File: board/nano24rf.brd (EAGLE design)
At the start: 17.8 x 50 mm, 26 parts, among them CN1 1X4-CLEANBIG, CN2 1X4-CLEANBIG, CN3 1X4-CLEANBIG, CN4 1X4-CLEANBIG

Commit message: before route
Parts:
- removed C1, C2: (no value), ATTAMI-V0.00:0805
- removed CN1, CN2, CN3, CN4, I2CPORT: 1X4-CLEANBIG, adafruit:1X04-CLEANBIG
- removed FET1, FET2, JP6: (no value), ATTAMI-V0.00:1X02_ROUND
- removed SJ1: JUMPER-PAD-3-2OF3_NC_BY_TRACE_SMALL, ATTAMI-V0.00:PAD-JUMPER-3-2OF3_NC_BY_TRACE_YES_SILK_FULL_BOX
- removed SJ2: (no value), ATTAMI-V0.00:PAD-JUMPER-3-2OF3_NC_BY_TRACE_YES_SILK_FULL_BOX
- removed SW1: (no value), microbuilder:SPST_SMT_19192
- removed U$2: NRF24, ATTAMI-V0.00:NRF24-2X4
- removed U2: (no value), microbuilder:SOT23-WIDE
- added D3, D4: (no value), dp_devices:DO-214AC
- added Q3, Q4: (no value), adafruit:SOT23-W
- added R5, R6: (no value), ATTAMI-V0.00:0805
- added U$6, U$8: 1X3SMD, nanorf24:FATPAD
- added U$7: 1X7-SMDPADS, nanorf24:SMD1,27-2,54
- JP3: device adafruit:1X01-CLEANBIG -> pinhead+:2X03_SMT
- moved R4 27.0 mm to (11.7, 45.8), turned to 0 degrees
- moved R3 26.3 mm to (6.48, 49.8), turned to 0 degrees
- moved R1 25.9 mm to (5.08, 38.7), turned to 0 degrees
- moved R2 23.7 mm to (12.6, 36.4), turned to 0 degrees
- moved Q1 23.2 mm to (5.08, 35.6)
- moved Q2 20.9 mm to (12.6, 33.3)
- moved JP3 14.4 mm to (8.89, 18.9)
- moved JP1 10.2 mm to (1.27, 38.0)
- moved JP2 10.2 mm to (16.5, 38.0)
- moved D2 5.44 mm to (10.2, 5.08), turned to 90 degrees
- moved D1 4.02 mm to (14.0, 5.08), turned to 90 degrees
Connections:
- removed net IRQ: U$2.IRQ
- removed net N$1 (its old number): D1.2, FET1.2, Q1.3
- removed net RAW: JP3.1, JP6.1, SW1.B
- removed net RX: CN4.3, JP2.14
- removed net TX: CN4.2, JP2.15
- removed net V-ADJ: C2.1, SJ1.1, U2.2
- removed net V-NRF: SJ1.2, U$2.VCC
- new net D10: JP2.3, R3.1
- new net D9: JP2.4, R4.1
- new net FET01: D1.2, Q1.3, U$8.P$1
- new net FET02: D2.2, Q2.3, U$8.P$3
- new net FET03: D3.2, Q3.3, U$6.P$1
- new net FET04: D4.2, Q4.3, U$6.P$3
- new net N$5: Q4.1, R4.2
- net 3V3: no longer R3.2, R4.2, SJ1.3, SJ2.1
- net 5V: now also JP3.2, R5.1; no longer C1.1, CN4.1, JP1.12, SJ2.3, U2.1
- net CE: now also JP2.6, U$7.2; no longer JP2.3, U$2.CE
- net CSN: now also JP2.5, U$7.3; no longer JP2.4, U$2.CSN
- net D3: no longer R1.1
- net D6: now also R1.1
- net GND: now also JP3.6, Q3.2, Q4.2, R6.1, U$7.4; no longer C1.2, C2.2, CN4.4, I2CPORT.4, JP6.2, U$2.GND, U2.3
- net MISO: now also JP3.1, U$7.5; no longer JP2.1, U$2.MISO
- net MOSI: now also JP3.4, U$7.6; no longer JP2.2, U$2.MOSI
- net N$4: now also Q3.1, R3.2; no longer D2.2, FET2.2, Q2.3
- net N$6: now also R5.2, R6.2, U$7.1; no longer I2CPORT.3, SJ2.2
- net RST: now also JP3.5; no longer JP2.13
- net SCK: now also JP3.3, U$7.7; no longer JP1.1, U$2.SCK
- net SCL: no longer I2CPORT.1, R4.1
- net SDA: no longer I2CPORT.2, R3.1
- net VIN: now also D3.1, D4.1, U$6.P$2, U$8.P$2; no longer FET1.1, FET2.1, SW1.C
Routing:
- net TX: track 42.3 -> 0.00 mm, vias 1 -> 0
- net 5V: track 41.4 -> 0.00 mm, vias 1 -> 0
- net RX: track 38.3 -> 0.00 mm, vias 1 -> 0
- net 3V3: track 31.5 -> 0.00 mm, vias 1 -> 0
- net VIN: track 29.5 -> 0.00 mm, vias 1 -> 0
- net D5: track 20.8 -> 0.00 mm
- net RAW: track 16.6 -> 0.00 mm
- net D3: track 14.5 -> 0.00 mm
- net SDA: track 13.4 -> 0.00 mm
- net MISO: track 13.4 -> 0.00 mm
- net SCL: track 13.2 -> 0.00 mm
- net MOSI: track 12.8 -> 0.00 mm
- net V-NRF: track 11.9 -> 0.00 mm
- net N$1 (its old number): track 11.4 -> 0.00 mm
- net N$4: track 10.7 -> 0.00 mm
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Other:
- board size 17.8 x 50 mm -> 17.8 x 57.7 mm
- board text added: "v2"
- board text removed: "3v3/5v"
- board text removed: "5V TX RX GND"
- board text removed: "OFF|ON"
- board text removed: "RAW"
- board text removed: "SCL"
- board text removed: "SDA"
- board text removed: "SEshenkar"
- board text removed: "gnd"
- board text removed: "this way"
- board text removed: "v1"
- board text removed: "vcc"

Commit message: added lib, need to fix volt div placment
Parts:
- JP3: device pinhead+:2X03_SMT -> nano24rf:2X03_SMT
- U$7: device nanorf24:SMD1,27-2,54 -> nano24rf:SMD1,27-2,54
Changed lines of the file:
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@@
 <attribute name="VALUE" x="13.335" y="57.023" size="0.4064" layer="27" ratio="10" rot="R270"/>
 </element>
-<element name="JP3" library="pinhead+" package="2X03_SMT" value="" x="8.89" y="18.923"/>
-<element name="U$7" library="nanorf24" package="SMD1,27-2,54" value="1X7-SMDPADS" x="14.859" y="9.271" smashed="yes" rot="R180"/>
+<element name="JP3" library="nano24rf" package="2X03_SMT" value="" x="8.89" y="18.923"/>
+<element name="U$7" library="nano24rf" package="SMD1,27-2,54" value="1X7-SMDPADS" x="14.859" y="9.271" smashed="yes" rot="R180"/>
 <element name="Q2" library="adafruit" package="SOT23-W" value="" x="12.573" y="33.274" smashed="yes" rot="MR180">
 <attribute name="VALUE" x="14.605" y="33.782" size="0.4064" layer="28" rot="MR180"/>

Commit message: ready to grb
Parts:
- moved R1 30.4 mm to (3.56, 8.33), flipped to the top, turned to 270 degrees
- moved R2 27.9 mm to (14.0, 8.59), flipped to the top, turned to 270 degrees
- moved R5 24.0 mm to (6.48, 43.0), flipped to the bottom
- moved R3 23.4 mm to (5.59, 26.4), turned to 180 degrees
- moved R6 19.3 mm to (11.4, 38.3), flipped to the bottom
- moved R4 16.7 mm to (11.8, 29.2)
- moved Q1 12.8 mm to (5.59, 22.8)
- moved D2 10.1 mm to (11.8, 15.1)
- moved D4 9.99 mm to (6.73, 15.1)
- moved Q2 7.56 mm to (12.1, 25.7)
- moved U$8 7.16 mm to (16.4, 6.81)
- moved U$6 7.16 mm to (1.27, 6.81)
- moved JP1 7.16 mm to (1.27, 30.8)
- moved JP2 7.16 mm to (16.5, 30.8)
- moved JP3 7.16 mm to (8.89, 11.8)
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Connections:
- removed net N$1: Q2.1, R2.2
- removed net N$2: Q1.1, R1.2
- removed net N$4: Q3.1, R3.2
- removed net N$5: Q4.1, R4.2
- net 5V: now also R1.1; no longer R5.1
- net D10: now also Q3.1, R5.2; no longer R3.1
- net D5: now also Q2.1, R4.2; no longer R2.1
- net D6: now also Q1.1, R3.2; no longer R1.1
- net D9: now also Q4.1, R6.2; no longer R4.1
- net GND: now also R2.1, R3.1, R4.1, R5.1
- net N$6: now also R1.2, R2.2; no longer R5.2, R6.2
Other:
- board size 17.8 x 57.7 mm -> 17.8 x 50 mm

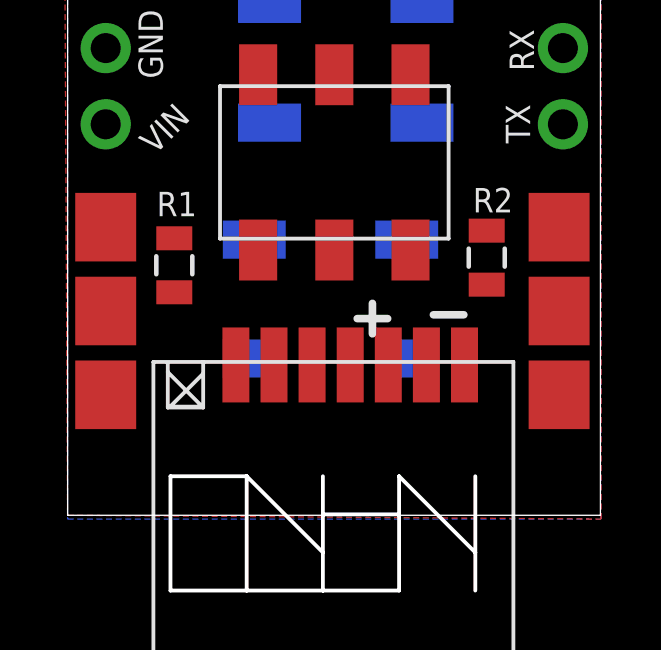
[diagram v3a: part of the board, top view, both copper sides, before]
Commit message: added FATPAD4
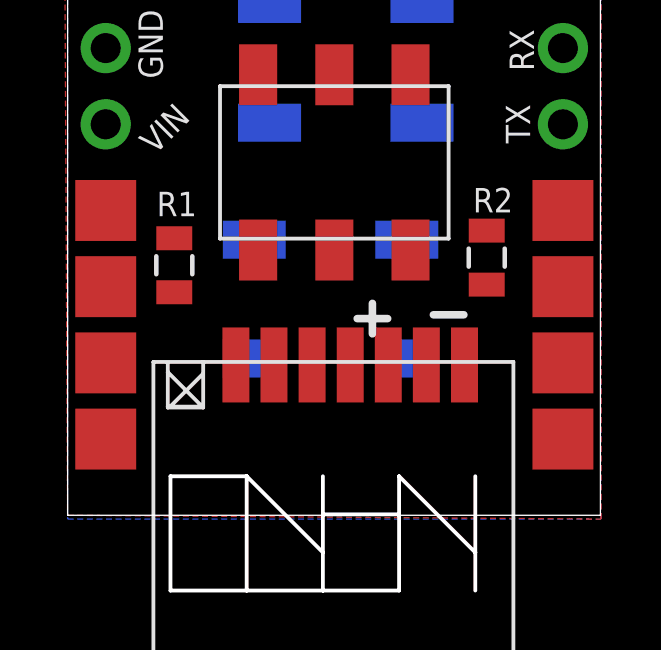
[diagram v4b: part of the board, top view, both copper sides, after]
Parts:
- U$6, U$8: value 1X3SMD -> FATPAD4; device nanorf24:FATPAD -> nano24rf:FATPAD4
- moved U$8 0.48 mm to (16.5, 6.35), turned to 270 degrees
- moved U$6 0.46 mm to (1.27, 6.35), turned to 270 degrees
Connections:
- net GND: now also U$6.P$4, U$8.P$4
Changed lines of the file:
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@@
 <setting verticaltext="up"/>
 </settings>
-<grid distance="50" unitdist="mil" unit="mil" style="lines" multiple="1" display="yes" altdistance="5" altunitdist="mil" altunit="mil"/>
+<grid distance="25" unitdist="mil" unit="mil" style="lines" multiple="1" display="yes" altdistance="5" altunitdist="mil" altunit="mil"/>
 <layers>
 <layer number="1" name="Top" color="4" fill="1" visible="yes" active="yes"/>
@@
 <attribute name="VALUE" x="3.731" y="12.565" size="1.27" layer="28" ratio="10" rot="MR90"/>
 </element>
-<element name="U$6" library="nanorf24" package="FATPAD" value="1X3SMD" x="1.27" y="6.81" rot="R90"/>
-<element name="U$8" library="nanorf24" package="FATPAD" value="1X3SMD" x="16.383" y="6.81" rot="R90"/>
+<element name="U$6" library="nano24rf" package="FATPAD4" value="FATPAD4" x="1.27" y="6.35" rot="R270"/>
+<element name="U$8" library="nano24rf" package="FATPAD4" value="FATPAD4" x="16.51" y="6.35" rot="R270"/>
 <element name="R1" library="ATTAMI-V0.00" package="0805" value="" x="3.556" y="8.334" smashed="yes" rot="R270">
 <attribute name="NAME" x="2.969" y="9.9695" size="0.8128" layer="25"/>
@@
 <contactref element="R6" pad="1"/>
 <contactref element="R3" pad="1"/>
+<contactref element="U$8" pad="P$4"/>
+<contactref element="U$6" pad="P$4"/>
+<wire x1="12.657" y1="36.431" x2="12.33" y2="38.306" width="0" layer="19" extent="16-16"/>
+<wire x1="7.577" y1="40.622" x2="12.33" y2="38.306" width="0" layer="19" extent="16-16"/>
+<wire x1="7.377" y1="43.005" x2="7.577" y2="40.622" width="0" layer="19" extent="16-16"/>
+<wire x1="1.27" y1="43.513" x2="7.377" y2="43.005" width="0" layer="19" extent="16-16"/>
+<wire x1="12.711" y1="29.162" x2="12.657" y2="36.431" width="0" layer="19" extent="16-16"/>
+<wire x1="13.165" y1="27.033" x2="12.711" y2="29.162" width="0" layer="19" extent="16-16"/>
+<wire x1="6.688" y1="24.065" x2="13.165" y2="27.033" width="0" layer="19" extent="16-16"/>
+<wire x1="4.688" y1="26.4" x2="6.688" y2="24.065" width="0" layer="19" extent="16-16"/>
+<wire x1="16.51" y1="20.653" x2="13.165" y2="27.033" width="0" layer="19" extent="16-16"/>
+<wire x1="11.43" y1="14.684" x2="16.51" y2="20.653" width="0" layer="19" extent="1-1"/>
+<wire x1="13.97" y1="9.488" x2="11.43" y2="14.684" width="0" layer="19" extent="1-1"/>
+<wire x1="16.51" y1="2.54" x2="13.97" y2="9.488" width="0" layer="19" extent="1-1"/>
+<wire x1="9.419" y1="5.011" x2="13.97" y2="9.488" width="0" layer="19" extent="1-1"/>
+<wire x1="1.27" y1="15.573" x2="6.688" y2="24.065" width="0" layer="19" extent="16-16"/>
+<wire x1="1.27" y1="2.54" x2="1.27" y2="15.573" width="0" layer="19" extent="1-1"/>
 </signal>
 <signal name="FET01">
@@
 <contactref element="D1" pad="2"/>
 <contactref element="U$8" pad="P$1"/>
-<wire x1="16.383" y1="4.016" x2="5.588" y2="21.465" width="0" layer="19" extent="1-16"/>
-<wire x1="11.303" y1="5.227" x2="16.383" y2="4.016" width="0" layer="19" extent="1-16"/>
+<wire x1="16.51" y1="10.16" x2="5.588" y2="21.465" width="0" layer="19" extent="1-16"/>
+<wire x1="11.303" y1="5.227" x2="16.51" y2="10.16" width="0" layer="19" extent="1-16"/>
 </signal>
 <signal name="D5">
@@
 <contactref element="U$6" pad="P$2"/>
 <contactref element="U$8" pad="P$2"/>
-<wire x1="11.303" y1="9.187" x2="16.383" y2="6.81" width="0" layer="19" extent="1-16"/>
+<wire x1="11.303" y1="9.187" x2="16.51" y2="7.62" width="0" layer="19" extent="1-16"/>
 <wire x1="11.811" y1="13.085" x2="11.303" y2="9.187" width="0" layer="19" extent="16-16"/>
 <wire x1="6.731" y1="13.085" x2="11.811" y2="13.085" width="0" layer="19" extent="16-16"/>
 <wire x1="6.223" y1="9.187" x2="6.731" y2="13.085" width="0" layer="19" extent="16-16"/>
-<wire x1="1.27" y1="6.81" x2="6.223" y2="9.187" width="0" layer="19" extent="1-16"/>
-<wire x1="1.27" y1="13.033" x2="1.27" y2="6.81" width="0" layer="19" extent="1-1"/>
+<wire x1="1.27" y1="7.62" x2="6.223" y2="9.187" width="0" layer="19" extent="1-16"/>
+<wire x1="1.27" y1="13.033" x2="1.27" y2="7.62" width="0" layer="19" extent="1-1"/>
 </signal>
 <signal name="RST">
@@
 <contactref element="D2" pad="2"/>
 <contactref element="U$8" pad="P$3"/>
-<wire x1="16.383" y1="9.604" x2="12.065" y2="24.433" width="0" layer="19" extent="1-16"/>
-<wire x1="11.811" y1="17.045" x2="16.383" y2="9.604" width="0" layer="19" extent="1-16"/>
+<wire x1="16.51" y1="5.08" x2="12.065" y2="24.433" width="0" layer="19" extent="1-16"/>
+<wire x1="11.811" y1="17.045" x2="16.51" y2="5.08" width="0" layer="19" extent="1-16"/>
 </signal>
 <signal name="FET03">
@@
 <contactref element="D3" pad="2"/>
 <contactref element="U$6" pad="P$1"/>
-<wire x1="1.27" y1="4.016" x2="6.477" y2="38.022" width="0" layer="19" extent="1-16"/>
-<wire x1="6.223" y1="5.227" x2="1.27" y2="4.016" width="0" layer="19" extent="1-16"/>
+<wire x1="1.27" y1="10.16" x2="6.477" y2="38.022" width="0" layer="19" extent="1-16"/>
+<wire x1="6.223" y1="5.227" x2="1.27" y2="10.16" width="0" layer="19" extent="1-16"/>
 </signal>
 <signal name="FET04">
@@
 <contactref element="D4" pad="2"/>
 <contactref element="U$6" pad="P$3"/>
-<wire x1="1.27" y1="9.604" x2="11.557" y2="33.831" width="0" layer="19" extent="1-16"/>
-<wire x1="6.731" y1="17.045" x2="1.27" y2="9.604" width="0" layer="19" extent="1-16"/>
+<wire x1="1.27" y1="5.08" x2="11.557" y2="33.831" width="0" layer="19" extent="1-16"/>
+<wire x1="6.731" y1="17.045" x2="1.27" y2="5.08" width="0" layer="19" extent="1-16"/>
 </signal>
 <signal name="N$6">

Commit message: after topor
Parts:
- moved Q3 5.18 mm to (6.22, 44.5), turned to 0 degrees
- moved R5 2.20 mm to (6.22, 40.8), turned to 180 degrees
- moved R1 0.68 mm to (3.81, 7.70)
- moved R2 0.40 mm to (14.1, 8.21)
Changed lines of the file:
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@@
 <attribute name="VALUE" x="8.811" y="12.565" size="1.27" layer="28" ratio="10" rot="MR90"/>
 </element>
-<element name="Q3" library="adafruit" package="SOT23-W" value="" x="6.477" y="39.322" smashed="yes" rot="MR180">
-<attribute name="VALUE" x="8.509" y="39.83" size="0.4064" layer="28" rot="MR180"/>
+<element name="Q3" library="adafruit" package="SOT23-W" value="" x="6.223" y="44.498" smashed="yes" rot="MR0">
+<attribute name="VALUE" x="4.191" y="43.99" size="0.4064" layer="28" rot="MR0"/>
 </element>
 <element name="D3" library="dp_devices" package="DO-214AC" value="" x="6.223" y="7.207" smashed="yes" rot="MR270">
@@
 <element name="U$6" library="nano24rf" package="FATPAD4" value="FATPAD4" x="1.27" y="6.35" rot="R270"/>
 <element name="U$8" library="nano24rf" package="FATPAD4" value="FATPAD4" x="16.51" y="6.35" rot="R270"/>
-<element name="R1" library="ATTAMI-V0.00" package="0805" value="" x="3.556" y="8.334" smashed="yes" rot="R270">
-<attribute name="NAME" x="2.969" y="9.9695" size="0.8128" layer="25"/>
-<attribute name="VALUE" x="2.159" y="9.35" size="0.4064" layer="27" rot="R270"/>
+<element name="R1" library="ATTAMI-V0.00" package="0805" value="" x="3.81" y="7.699" smashed="yes" rot="R270">
+<attribute name="NAME" x="3.223" y="9.3345" size="0.8128" layer="25"/>
+<attribute name="VALUE" x="2.413" y="8.715" size="0.4064" layer="27" rot="R270"/>
 </element>
-<element name="R2" library="ATTAMI-V0.00" package="0805" value="" x="13.97" y="8.588" smashed="yes" rot="R270">
-<attribute name="NAME" x="13.51" y="10.0965" size="0.8128" layer="25"/>
-<attribute name="VALUE" x="12.573" y="9.604" size="0.4064" layer="27" rot="R270"/>
+<element name="R2" library="ATTAMI-V0.00" package="0805" value="" x="14.097" y="8.207" smashed="yes" rot="R270">
+<attribute name="NAME" x="13.637" y="9.7155" size="0.8128" layer="25"/>
+<attribute name="VALUE" x="12.7" y="9.223" size="0.4064" layer="27" rot="R270"/>
 </element>
 <element name="R4" library="ATTAMI-V0.00" package="0805" value="" x="11.811" y="29.162" smashed="yes" rot="MR0">
-<attribute name="NAME" x="10.414" y="30.8455" size="0.8128" layer="26" rot="MR180"/>
+<attribute name="NAME" x="13.3505" y="28.448" size="0.8128" layer="26" rot="MR90"/>
 <attribute name="VALUE" x="12.827" y="27.765" size="0.4064" layer="28" rot="MR0"/>
 </element>
 <element name="R3" library="ATTAMI-V0.00" package="0805" value="" x="5.588" y="26.4" smashed="yes" rot="MR180">
-<attribute name="NAME" x="6.985" y="27.3845" size="0.8128" layer="26" rot="MR0"/>
+<attribute name="NAME" x="7.9215" y="27.178" size="0.8128" layer="26" rot="MR270"/>
 <attribute name="VALUE" x="4.572" y="27.797" size="0.4064" layer="28" rot="MR180"/>
 </element>
 <element name="R6" library="ATTAMI-V0.00" package="0805" value="" x="11.43" y="38.306" smashed="yes" rot="MR0">
-<attribute name="NAME" x="10.033" y="40.1165" size="0.8128" layer="26" rot="MR180"/>
+<attribute name="NAME" x="12.9695" y="37.719" size="0.8128" layer="26" rot="MR90"/>
 <attribute name="VALUE" x="12.446" y="36.909" size="0.4064" layer="28" rot="MR0"/>
 </element>
-<element name="R5" library="ATTAMI-V0.00" package="0805" value="" x="6.477" y="43.005" smashed="yes" rot="MR0">
-<attribute name="NAME" x="5.334" y="44.8155" size="0.8128" layer="26" rot="MR180"/>
-<attribute name="VALUE" x="7.493" y="41.608" size="0.4064" layer="28" rot="MR0"/>
+<element name="R5" library="ATTAMI-V0.00" package="0805" value="" x="6.223" y="40.815" smashed="yes" rot="MR180">
+<attribute name="NAME" x="8.6205" y="41.402" size="0.8128" layer="26" rot="MR270"/>
+<attribute name="VALUE" x="5.207" y="42.212" size="0.4064" layer="28" rot="MR180"/>
 </element>
 </elements>
@@
 <contactref element="U$8" pad="P$4"/>
 <contactref element="U$6" pad="P$4"/>
-<wire x1="12.657" y1="36.431" x2="12.33" y2="38.306" width="0" layer="19" extent="16-16"/>
-<wire x1="7.577" y1="40.622" x2="12.33" y2="38.306" width="0" layer="19" extent="16-16"/>
-<wire x1="7.377" y1="43.005" x2="7.577" y2="40.622" width="0" layer="19" extent="16-16"/>
-<wire x1="1.27" y1="43.513" x2="7.377" y2="43.005" width="0" layer="19" extent="16-16"/>
-<wire x1="12.711" y1="29.162" x2="12.657" y2="36.431" width="0" layer="19" extent="16-16"/>
-<wire x1="13.165" y1="27.033" x2="12.711" y2="29.162" width="0" layer="19" extent="16-16"/>
-<wire x1="6.688" y1="24.065" x2="13.165" y2="27.033" width="0" layer="19" extent="16-16"/>
-<wire x1="4.688" y1="26.4" x2="6.688" y2="24.065" width="0" layer="19" extent="16-16"/>
-<wire x1="16.51" y1="20.653" x2="13.165" y2="27.033" width="0" layer="19" extent="16-16"/>
-<wire x1="11.43" y1="14.684" x2="16.51" y2="20.653" width="0" layer="19" extent="1-1"/>
-<wire x1="13.97" y1="9.488" x2="11.43" y2="14.684" width="0" layer="19" extent="1-1"/>
-<wire x1="16.51" y1="2.54" x2="13.97" y2="9.488" width="0" layer="19" extent="1-1"/>
-<wire x1="9.419" y1="5.011" x2="13.97" y2="9.488" width="0" layer="19" extent="1-1"/>
-<wire x1="1.27" y1="15.573" x2="6.688" y2="24.065" width="0" layer="19" extent="16-16"/>
-<wire x1="1.27" y1="2.54" x2="1.27" y2="15.573" width="0" layer="19" extent="1-1"/>
 </signal>
 <signal name="FET01">
@@
 <contactref element="JP3" pad="2"/>
 <contactref element="R1" pad="1"/>
-<wire x1="3.556" y1="9.234" x2="6.35" y2="14.684" width="0" layer="19" extent="1-1"/>
+<wire x1="3.81" y1="8.599" x2="6.35" y2="14.684" width="0" layer="19" extent="1-1"/>
 </signal>
 <signal name="SDA">
@@
 <contactref element="U$6" pad="P$2"/>
 <contactref element="U$8" pad="P$2"/>
-<wire x1="11.303" y1="9.187" x2="16.51" y2="7.62" width="0" layer="19" extent="1-16"/>
-<wire x1="11.811" y1="13.085" x2="11.303" y2="9.187" width="0" layer="19" extent="16-16"/>
+<wire x1="11.303" y1="9.187" x2="11.811" y2="13.085" width="0" layer="19" extent="16-16"/>
 <wire x1="6.731" y1="13.085" x2="11.811" y2="13.085" width="0" layer="19" extent="16-16"/>
 <wire x1="6.223" y1="9.187" x2="6.731" y2="13.085" width="0" layer="19" extent="16-16"/>
 <wire x1="1.27" y1="7.62" x2="6.223" y2="9.187" width="0" layer="19" extent="1-16"/>
 <wire x1="1.27" y1="13.033" x2="1.27" y2="7.62" width="0" layer="19" extent="1-1"/>
+<wire x1="16.51" y1="7.62" x2="11.303" y2="9.187" width="0" layer="19" extent="1-16"/>
 </signal>
 <signal name="RST">
@@
 <contactref element="Q3" pad="1"/>
 <contactref element="R5" pad="2"/>
-<wire x1="5.577" y1="43.005" x2="16.51" y2="43.513" width="0" layer="19" extent="16-16"/>
-<wire x1="5.377" y1="40.622" x2="5.577" y2="43.005" width="0" layer="19" extent="16-16"/>
+<wire x1="7.323" y1="43.198" x2="16.51" y2="43.513" width="0" layer="19" extent="16-16"/>
+<wire x1="7.123" y1="40.815" x2="7.323" y2="43.198" width="0" layer="19" extent="16-16"/>
 </signal>
 <signal name="D9">
@@
 <contactref element="D2" pad="2"/>
 <contactref element="U$8" pad="P$3"/>
-<wire x1="16.51" y1="5.08" x2="12.065" y2="24.433" width="0" layer="19" extent="1-16"/>
-<wire x1="11.811" y1="17.045" x2="16.51" y2="5.08" width="0" layer="19" extent="1-16"/>
+<wire x1="11.811" y1="17.045" x2="12.065" y2="24.433" width="0" layer="19" extent="16-16"/>
+<wire x1="16.51" y1="5.08" x2="11.811" y2="17.045" width="0" layer="19" extent="1-16"/>
 </signal>
 <signal name="FET03">
@@
 <contactref element="D3" pad="2"/>
 <contactref element="U$6" pad="P$1"/>
-<wire x1="1.27" y1="10.16" x2="6.477" y2="38.022" width="0" layer="19" extent="1-16"/>
+<wire x1="1.27" y1="10.16" x2="6.223" y2="45.798" width="0" layer="19" extent="1-16"/>
 <wire x1="6.223" y1="5.227" x2="1.27" y2="10.16" width="0" layer="19" extent="1-16"/>
 </signal>
@@
 <contactref element="D4" pad="2"/>
 <contactref element="U$6" pad="P$3"/>
-<wire x1="1.27" y1="5.08" x2="11.557" y2="33.831" width="0" layer="19" extent="1-16"/>
-<wire x1="6.731" y1="17.045" x2="1.27" y2="5.08" width="0" layer="19" extent="1-16"/>
+<wire x1="6.731" y1="17.045" x2="11.557" y2="33.831" width="0" layer="19" extent="16-16"/>
+<wire x1="1.27" y1="5.08" x2="6.731" y2="17.045" width="0" layer="19" extent="1-16"/>
 </signal>
 <signal name="N$6">
@@
 <contactref element="U$7" pad="1"/>
 <contactref element="R2" pad="2"/>
-<wire x1="3.556" y1="7.434" x2="13.97" y2="7.688" width="0" layer="19" extent="1-1"/>
-<wire x1="13.229" y1="5.011" x2="13.97" y2="7.688" width="0" layer="19" extent="1-1"/>
+<wire x1="13.229" y1="5.011" x2="14.097" y2="7.307" width="0" layer="19" extent="1-1"/>
+<wire x1="3.81" y1="6.799" x2="13.229" y2="5.011" width="0" layer="19" extent="1-1"/>
 </signal>
 </signals>

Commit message: another go on the topoR
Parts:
- moved D3 16.4 mm to (6.06, 23.6), turned to 0 degrees
- moved D1 11.2 mm to (11.8, 18.4), turned to 180 degrees
- moved D4 9.86 mm to (11.6, 23.6), turned to 180 degrees
- moved Q1 7.44 mm to (6.60, 30.1)
- moved R3 7.20 mm to (6.48, 33.5), turned to 0 degrees
- moved D2 6.37 mm to (6.40, 18.4), turned to 0 degrees
- moved Q3 5.83 mm to (6.73, 38.7), turned to 180 degrees
- moved Q2 3.39 mm to (11.3, 29.0)
- moved R4 3.34 mm to (11.3, 32.5)
- moved R6 3.05 mm to (11.3, 41.4)
- moved Q4 2.68 mm to (11.3, 37.8)
- moved R5 1.45 mm to (6.86, 42.1), turned to 0 degrees
- moved R1 0.77 mm to (3.68, 8.46)
- moved R2 0.28 mm to (13.8, 8.33)
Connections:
- new net S$1: U$6.P$4, U$7.4
- net GND: no longer U$6.P$4, U$7.4
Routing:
- removed copper zone on layer 1, net GND
- removed copper zone on layer 16, net GND
